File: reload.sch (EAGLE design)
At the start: 20 parts, among them IC1 MCP6002, IC2 LP2950Z, Q1 BTS117

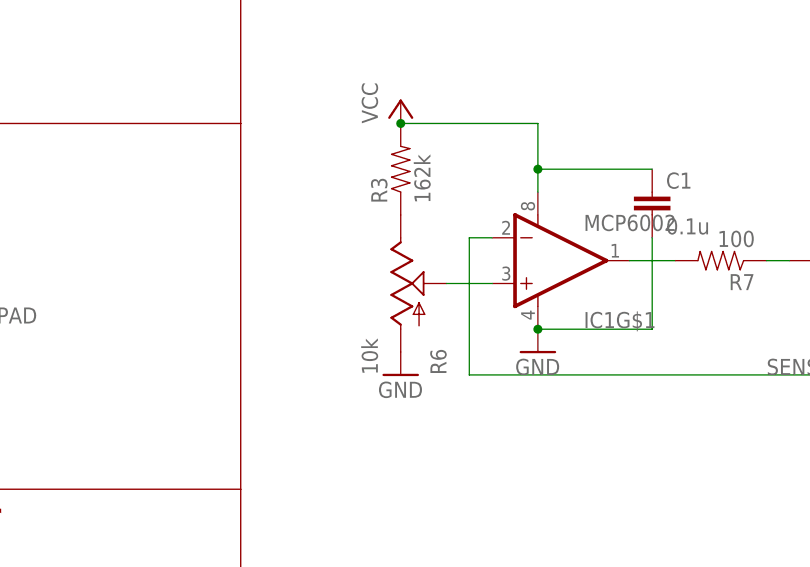
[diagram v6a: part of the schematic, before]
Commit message: Board rearrangement for spring terminals, better pot placement.
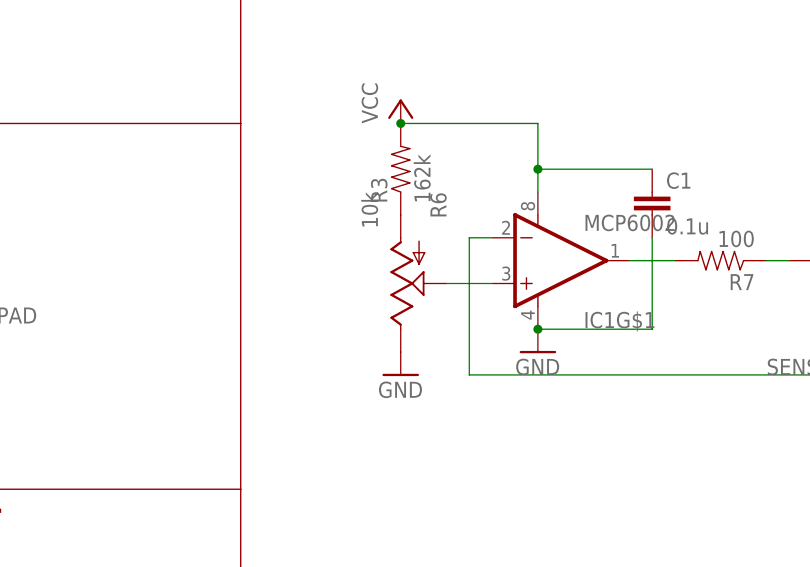
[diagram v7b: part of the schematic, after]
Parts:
- JP1: device SparkFun-Connectors:M025MM -> nickparts:M02
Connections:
- removed net N$3: R3.1, R6.E
- new net N$2: R3.1, R6.A
- net GND: now also R6.E; no longer R6.A
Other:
- moved on the sheet: R6
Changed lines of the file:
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@@
 <part name="J1" library="SparkFun-Connectors" deviceset="BANANA_CONN" device=""/>
 <part name="J2" library="SparkFun-Connectors" deviceset="BANANA_CONN" device=""/>
-<part name="JP1" library="SparkFun-Connectors" deviceset="M02" device="5MM"/>
+<part name="JP1" library="nickparts" deviceset="M02" device=""/>
 <part name="P+1" library="supply1" deviceset="V+" device=""/>
 <part name="GND1" library="supply1" deviceset="GND" device=""/>
@@
 <instance part="GND1" gate="1" x="147.32" y="76.2"/>
 <instance part="GND2" gate="1" x="111.76" y="93.98"/>
-<instance part="R6" gate="G$1" x="96.52" y="101.6"/>
+<instance part="R6" gate="G$1" x="96.52" y="101.6" rot="MR180"/>
 <instance part="GND3" gate="1" x="96.52" y="91.44"/>
 <instance part="R3" gate="G$1" x="96.52" y="114.3" rot="R90"/>
@@
 </segment>
 <segment>
-<pinref part="R6" gate="G$1" pin="A"/>
-<pinref part="GND3" gate="1" pin="GND"/>
-</segment>
-<segment>
 <pinref part="GND4" gate="1" pin="GND"/>
 <wire x1="48.26" y1="27.94" x2="48.26" y2="30.48" width="0.1524" layer="91"/>
@@
 <junction x="43.18" y="139.7"/>
 </segment>
-</net>
-<net name="N$3" class="0">
-<segment>
+<segment>
+<pinref part="GND3" gate="1" pin="GND"/>
 <pinref part="R6" gate="G$1" pin="E"/>
-<pinref part="R3" gate="G$1" pin="1"/>
 </segment>
 </net>
@@
 </segment>
 </net>
+<net name="N$2" class="0">
+<segment>
+<pinref part="R3" gate="G$1" pin="1"/>
+<pinref part="R6" gate="G$1" pin="A"/>
+</segment>
+</net>

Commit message: SMD respin
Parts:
- removed D1: (no value), SparkFun-DiscreteSemi:DIODE1N4148
- removed IC1: MCP6002, SparkFun-AnalogIC:LM358
- removed IC2: LP2950Z, linear:LP2950Z
- removed TP1, TP2: (no value), microbuilder:TESTPOINT0.1"
- added C4: 0.1u, SparkFun-Passives:CAP0805
- added IC3: OPAMP-DUALU, SparkFun-AnalogIC:OPAMP-DUALU
- added R8: 10k 1%, SparkFun-Passives:RESISTOR0805-RES
- added U$1: V_REG_MIC2920, SparkFun-PowerIC:V_REG_MIC2920
- C1: device SparkFun-Passives:CAPPTH -> SparkFun-Passives:CAP0805
- C2: device SparkFun-Passives:CAP_POLPTH2 -> SparkFun-Passives:CAP_POLC
- C3: device SparkFun-Passives:CAPPTH1 -> SparkFun-Passives:CAP0805
- JP1: device nickparts:M02 -> SparkFun-Connectors:M031X03_NO_SILK
- R1: device SparkFun-Passives:RESISTORPTH-1W -> SparkFun-Passives:RESISTOR2512
- R3, R4, R5, R7: device SparkFun-Passives:RESISTORAXIAL-0.3 -> SparkFun-Passives:RESISTOR0805-RES
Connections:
- removed net N$8: C3.1, D1.C, IC2.I
- new net N$3: Q1.S, R1.2, R8.1
- net GND: now also IC3A.V-, U$1.GND; no longer IC1G$1.V-, IC2.GND, TP2.P$1
- net IREF: now also IC3B.OUT, JP1.2; no longer IC1G$2.OUT, TP1.P$1
- net N$1: now also C4.1, IC3A.OUT; no longer IC1G$1.OUT
- net N$4: now also IC3A.+IN; no longer IC1G$1.+IN
- net N$5: now also IC3B.-IN; no longer IC1G$2.-IN
- net SENSE: now also C4.2, IC3A.-IN, IC3B.+IN, R8.2; no longer IC1G$1.-IN, IC1G$2.+IN, Q1.S, R1.2
- net V+: now also C3.1, JP1.3, U$1.IN; no longer D1.A, JP1.2
- net VCC: now also IC3A.V+, U$1.OUT; no longer IC1G$1.V+, IC2.O
